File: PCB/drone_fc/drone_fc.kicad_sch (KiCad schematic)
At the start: 35 parts, among them J1 USB_C_Receptacle_USB2.0_16P, J2 Conn_01x04_Socket, J3 Conn_01x07_Socket, U1 nRF52840, U2 USBLC6-2SC6, U3 ICM-20948, U4 MCP1703AT-3302E/DB, X1 32MHz

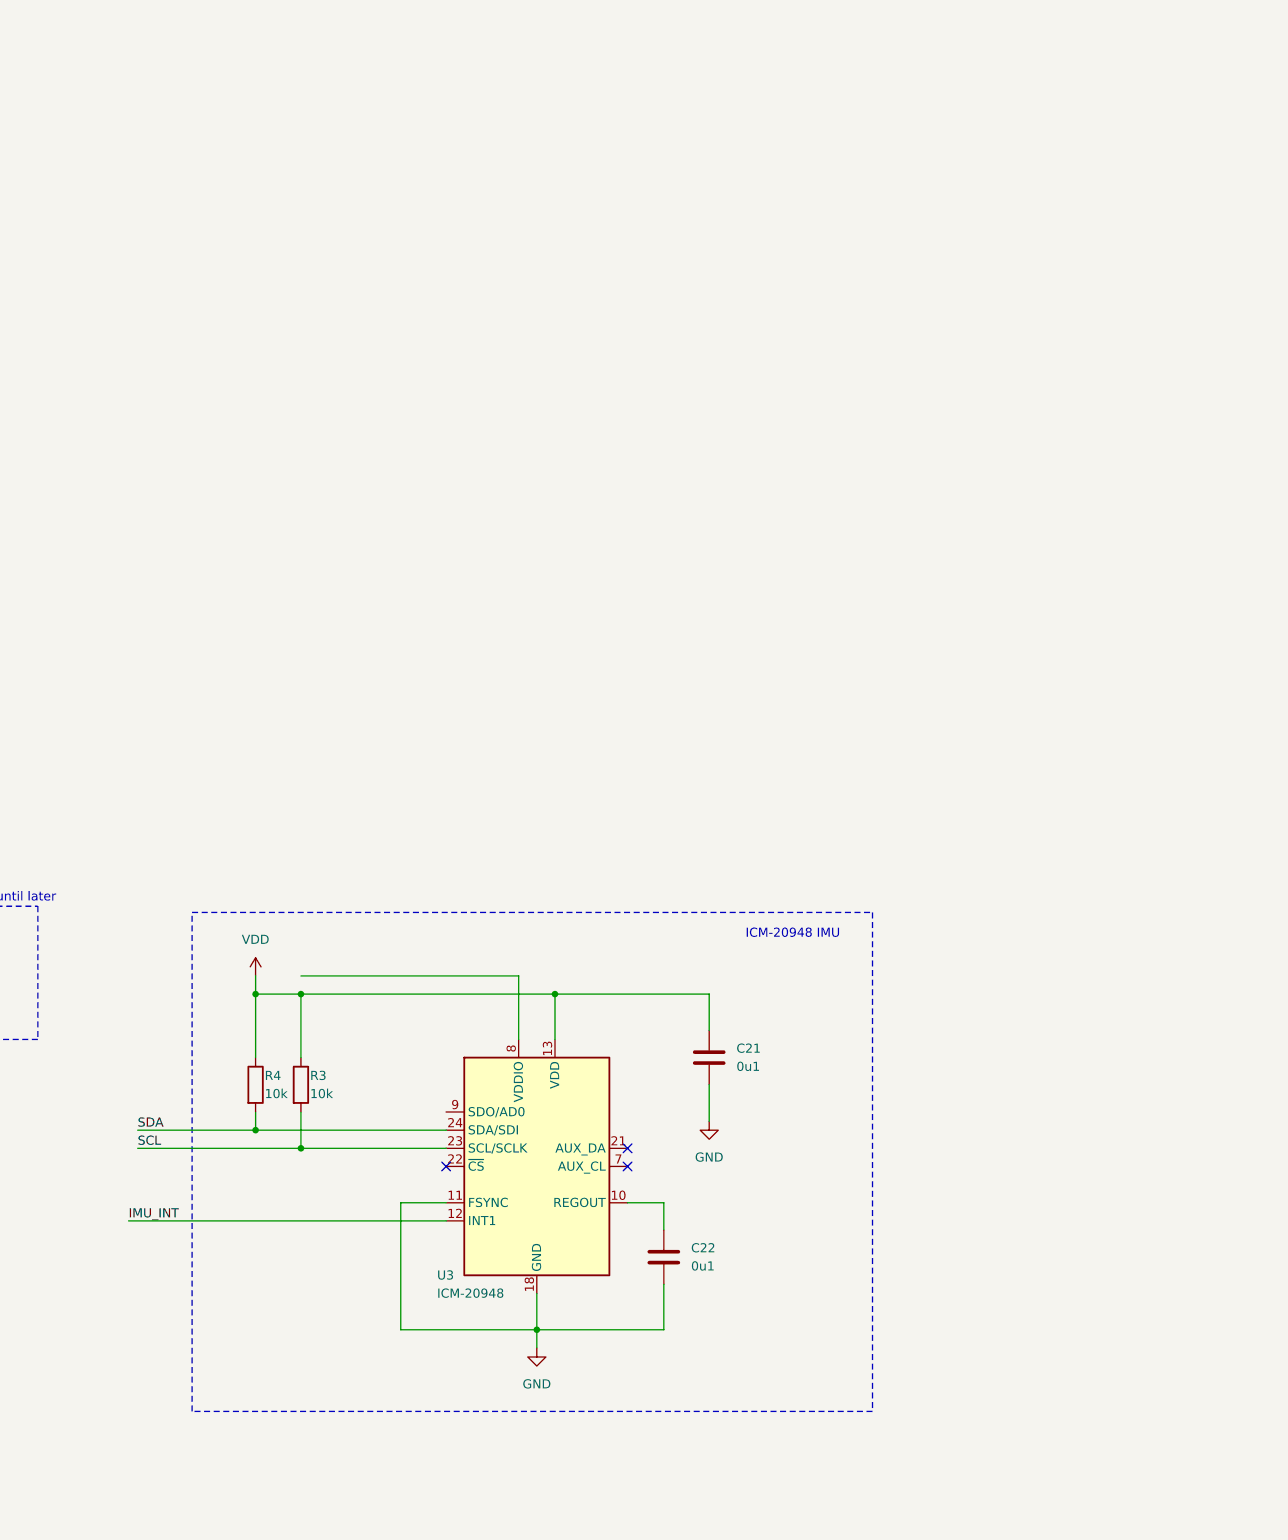
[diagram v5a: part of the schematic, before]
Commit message: Adjusted PCB size to more accurately match the ESC and added MOSFETs to provide logic level shifting on the I2C lines between the uC and IMU (thanks Adafruit and Digikey)
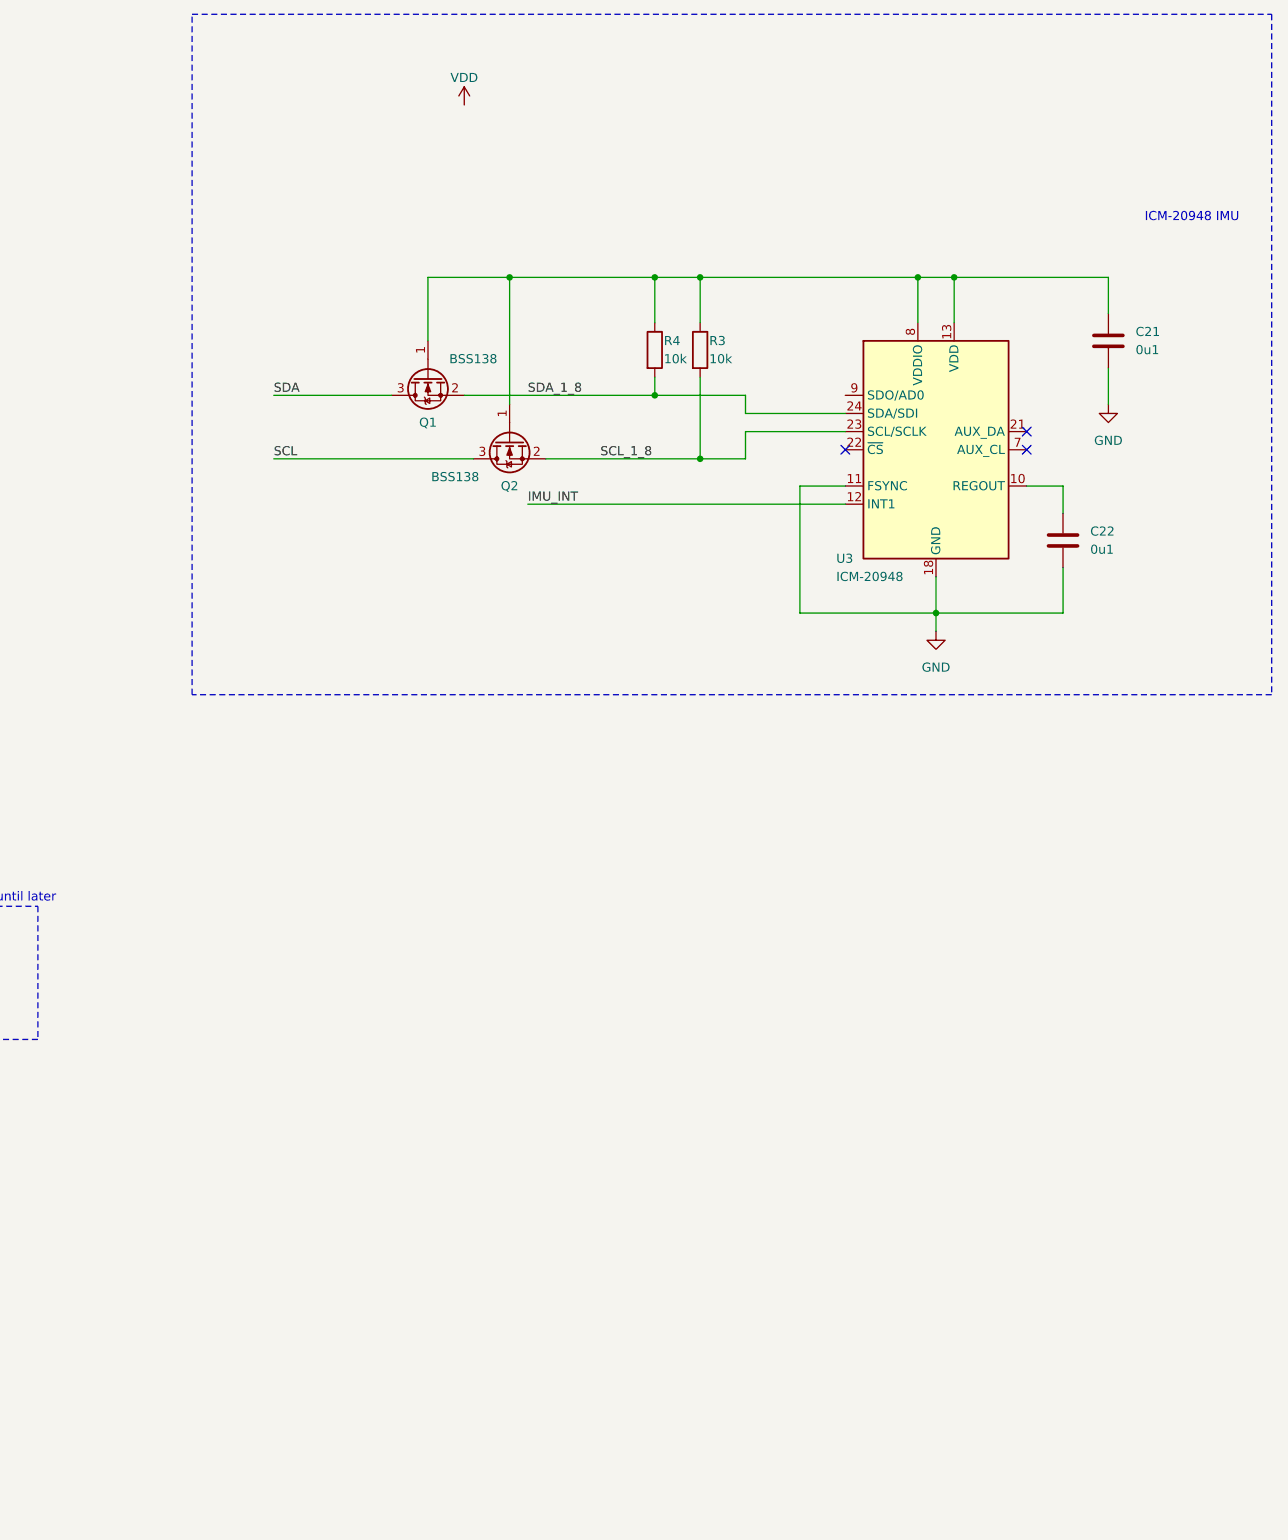
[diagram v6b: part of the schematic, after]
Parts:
- added Q1, Q2: BSS138, Package_TO_SOT_SMD:SOT-23, symbol Transistor_FET:BSS138
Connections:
- net SCL: now also Q2.3 (D); no longer R3.2, U3.23 (SCL/SCLK)
- net SDA: now also Q1.3 (D); no longer R4.2, U3.24 (SDA/SDI)
- net VDD: no longer C21.1, R3.1, R4.1, U3.13 (VDD)
- net at U3.8 (VDDIO): now also C21.1, R3.1, R4.1, U3.13 (VDD), Q1.1 (G), Q2.1 (G)
- new net SCL_1_8: Q2.2 (S), R3.2, U3.23 (SCL/SCLK)
- new net SDA_1_8: Q1.2 (S), R4.2, U3.24 (SDA/SDI)
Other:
- moved on the sheet: C21, C22, R3, R4, U3

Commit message: Many new additions but importantly new MOSFETs for logic shifting (2 in 1 chip), some models to go with footprints on the JST connectors, and a footprint for battery power. Why did I choose such a small board size as my first real PCB
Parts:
- removed Q1, Q2: BSS138, Package_TO_SOT_SMD:SOT-23, symbol Transistor_FET:BSS138
- added C23, C3: 1u, symbol Device:C
- added Q1: BSD840N, BSD840N:PG-SOT-363-DUAL-N_INF, symbol BSD840N:BSD840NH6327XTSA1_1
- added R5, R6: 10k, symbol Device:R
- added U5: LP5907MFX-1.8, Package_TO_SOT_SMD:SOT-23-5, symbol Regulator_Linear:LP5907MFX-1.8
- BT1: footprint (none) -> MiscPads:Pad
- J2: footprint (none) -> Connector_JST:JST_SH_SM04B-SRSS-TB_1x04-1MP_P1.00mm_Horizontal; Link (none) -> https://www.digikey.com/en/products/detail/jst-sales-americ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; Manufacturer (none) -> JST Sales America Inc.
- J3: value Conn_01x07_Socket -> Conn_01x08_Socket; footprint (none) -> Connector_JST:JST_SH_SM08B-SRSS-TB_1x08-1MP_P1.00mm_Horizontal; symbol Connector:Conn_01x07_Socket -> Connector:Conn_01x08_Socket; Link (none) -> https://www.digikey.com/en/products/detail/jst-sales-americ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; Manufacturer (none) -> JST Sales America Inc.
- U1: footprint nRF52840:nRF52840 -> Package_DFN_QFN:Nordic_AQFN-73-1EP_7x7mm_P0.5mm
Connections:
- net GND: now also J2.1 (Pin_1), J3.8 (Pin_8), C23.2, C3.2, U5.2 (GND)
- net SCL: now also J2.3 (Pin_3), U1.J1 (AIN2/P0.04), Q1.4, R6.2
- net SCL_1_8: now also Q1.3
- net SDA: now also J2.4 (Pin_4), U1.G1 (P0.26), Q1.1, R5.2
- net SDA_1_8: now also Q1.6
- net VDD: now also J2.2 (Pin_2), C3.1, R5.1, R6.1, U5.1 (IN), U5.3 (EN)
- net +1V8: now reaches C21.1, R3.1, R4.1, U3.13 (VDD), U3.8 (VDDIO)
- net +1V8: now also C23.1, Q1.2, Q1.5, U5.5 (OUT)
- net M1: now reaches J3.1 (Pin_1)
- net M2: now reaches J3.2 (Pin_2)
- net M3: now reaches J3.3 (Pin_3)
- net M4: now reaches J3.4 (Pin_4)
- net TEL: now reaches J3.5 (Pin_5)
- net CUR: now reaches J3.6 (Pin_6)
- net VBAT: now reaches J3.7 (Pin_7)
- net IMU_INT renamed IMU_INT_1_8
- no-connect marks 9 -> 11
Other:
- note added: "+3.3V"
- note added: "Contains 3.3 - 1.8 V regulator and logic shifting for I2C"
- note added: "JST Sockets for ESC and Distance sensor connection"
- note added: "This might need to change"
- note added: "Will need another MOSFET for this"
- moved on the sheet: C1, C10, C11, C12, C13, C14, C15, C16, C17, C18, C19, C2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

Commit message: New parts and footprints for existing resistors. Still some work to be done on checking battery voltage and PCB layout
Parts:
- removed Q1: BSD840N, BSD840N:PG-SOT-363-DUAL-N_INF, symbol BSD840N:BSD840NH6327XTSA1_1
- added C24, C25: 1u, Capacitor_SMD:C_0603_1608Metric, symbol Device:C
- added D1: D_Schottky, Diode_SMD:Nexperia_CFP3_SOD-123W, symbol Device:D_Schottky
- added SW1: PTS820J25M, SW2_PTS820J25MSMTRLFS_CNK, symbol PTS820J25MSMTR:PTS820J25MSMTRLFS
- added U6: TCA9517A, symbol TCA9517A:TCA95177A
- C1, C15, C19, C2, C20, C23, C3, C4, C5, C6, C7, C8, C9: footprint (none) -> Capacitor_SMD:C_0603_1608Metric
- C10, C14, C18: footprint (none) -> Capacitor_SMD:C_0402_1005Metric; now not fitted
- C11, C12, C13, C16, C17, C21, C22: footprint (none) -> Capacitor_SMD:C_0402_1005Metric
- L1: footprint (none) -> Inductor_SMD:L_0402_1005Metric
- R1, R2: value R -> 4k7; footprint (none) -> Resistor_SMD:R_0603_1608Metric
- R3, R4, R5, R6: footprint (none) -> Resistor_SMD:R_0603_1608Metric
- X1: footprint (none) -> Crystal:Crystal_SMD_2016-4Pin_2.0x1.6mm
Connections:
- net +15V: now also D1.1 (K)
- net +1V8: now also C24.1, U6.1 (VCCA)
- net D+: now also U2.3 (I/O2); no longer U2.1 (I/O1)
- net D-: now also U2.1 (I/O1); no longer U2.3 (I/O2)
- net DR+: now also U2.4 (I/O2); no longer U2.6 (I/O1)
- net DR-: now also U2.6 (I/O1); no longer U2.4 (I/O2)
- net GND: now also C24.2, C25.2, SW1.2, U6.4 (GND)
- net M1: now also U1.A20 (P1.10)
- net M2: now also U1.A16 (P1.13)
- net M3: now also U1.A14 (P1.15)
- net M4: now also U1.A12 (AIN0/P0.02)
- net SCL: now also U6.7 (SCLB)
- net SDA: now also U6.6 (SDAB)
- net VBAT: now also U1.A10 (AIN5/P0.29)
- net VBUS: now also D1.2 (A); no longer U1.Y2 (VDDH)
- net VDD: no longer C1.1, C15.1, C20.1, C3.1, C4.1, C6.1, C7.1, J2.2 (Pin_2), U1.A22 (VDD), U1.AD14 (VDD), U1.AD23 (VDD), U1.B1 (VDD), U1.W1 (VDD), U2.5 (VBUS), U4.3 (VO), U5.1 (IN), U5.3 (EN)
- net SWDCLK: now reaches U1.AA24 (SWDCLK)
- net at U1.AC13 (P0.18/~{RESET}): now also SW1.1
- net SWDIO: now reaches U1.AC24 (SWDIO)
- net SCL_1_8: no longer names the net of U3.23 (SCL/SCLK)
- net SCL_1_8: now also R4.2, U6.2 (SCLA); no longer R3.2
- net SDA_1_8: no longer names the net of U3.24 (SDA/SDI)
- net SDA_1_8: now also R3.2, U6.3 (SDAA); no longer R4.2
- new net 3V3: C1.1, C15.1, C20.1, C25.1, C3.1, C4.1, C6.1, C7.1, J2.2 (Pin_2), U1.A22 (VDD), U1.AD14 (VDD), U1.AD23 (VDD), U1.B1 (VDD), U1.W1 (VDD), U1.Y2 (VDDH), U2.5 (VBUS), U4.3 (VO), U5.1 (IN), U5.3 (EN), U6.5 (EN), U6.8 (VCCB)
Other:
- note added: "Input power step-down Allows power through USB and battery"
- note added: "Will need a MOSFET for this"
- note removed: "+3.3V"
- note removed: "This might need to change"
- note removed: "Will need another MOSFET for this"
- moved on the sheet: BT1, C1, C11, C12, C13, C15, C16, C17, C19, C2, C20, C21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
